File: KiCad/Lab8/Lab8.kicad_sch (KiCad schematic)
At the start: 24 parts, among them M1 Motor, M2 Motor, SW1 Reset, U1 PIC32MX170F256B, U2 74ACT244, U2 SN754410NE

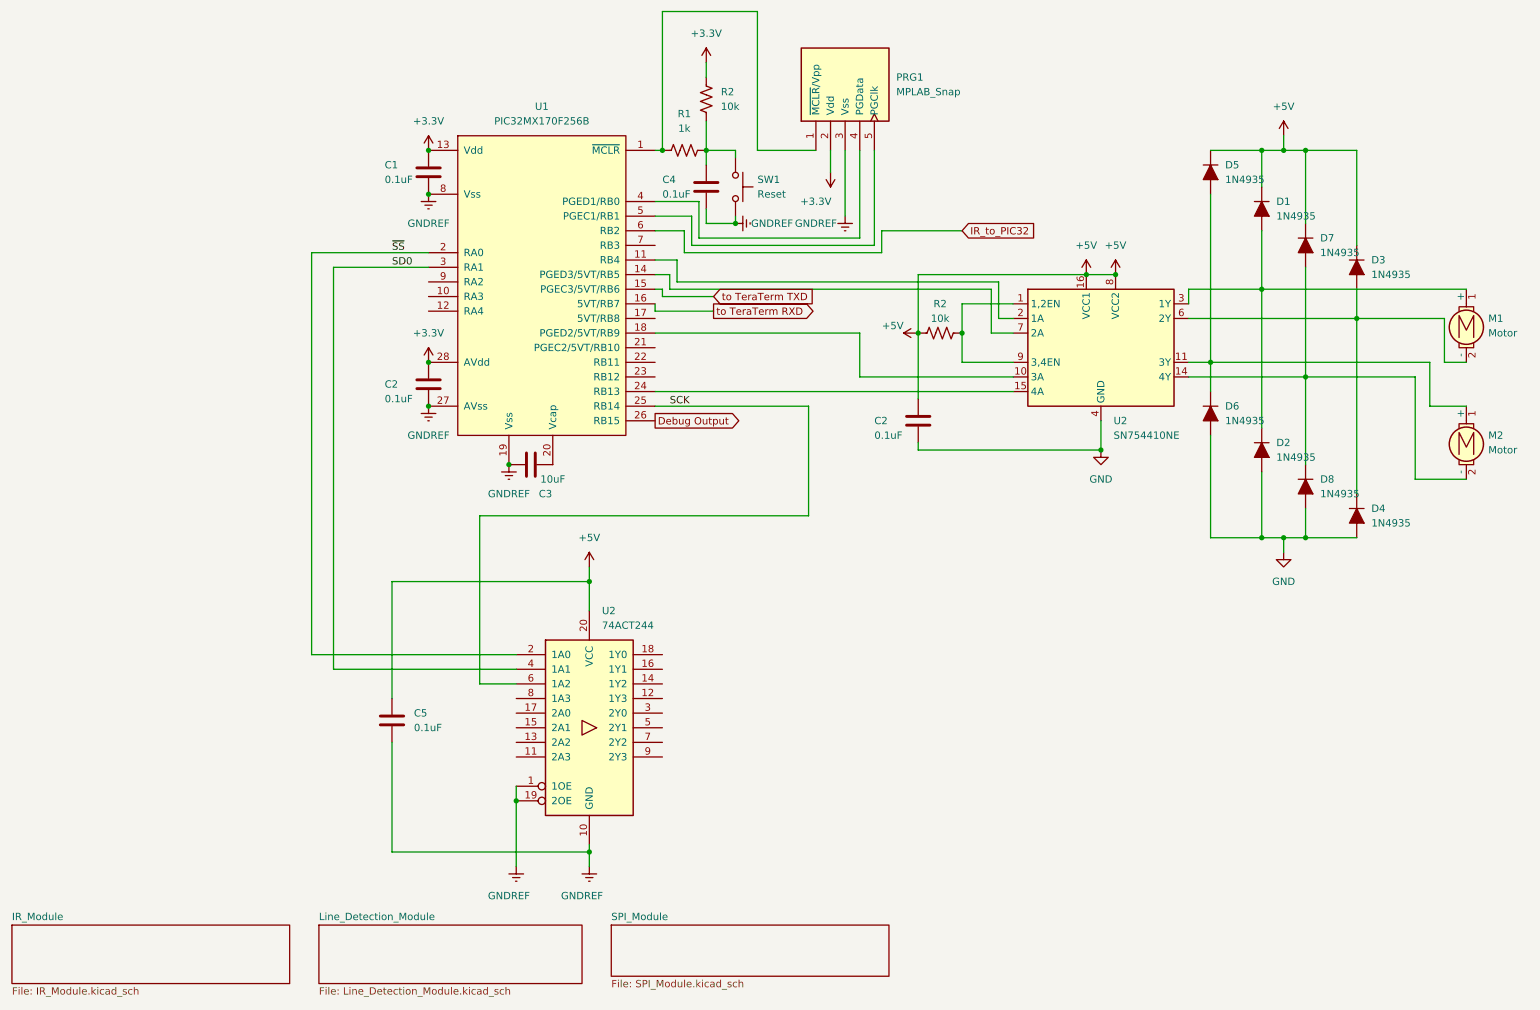
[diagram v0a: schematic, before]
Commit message: Revert "Revert "Update SPI wiring and implement line detection capture""
This reverts commit 9eb00a7cf1ff2e7c6ae798789d116206cfe13d70.
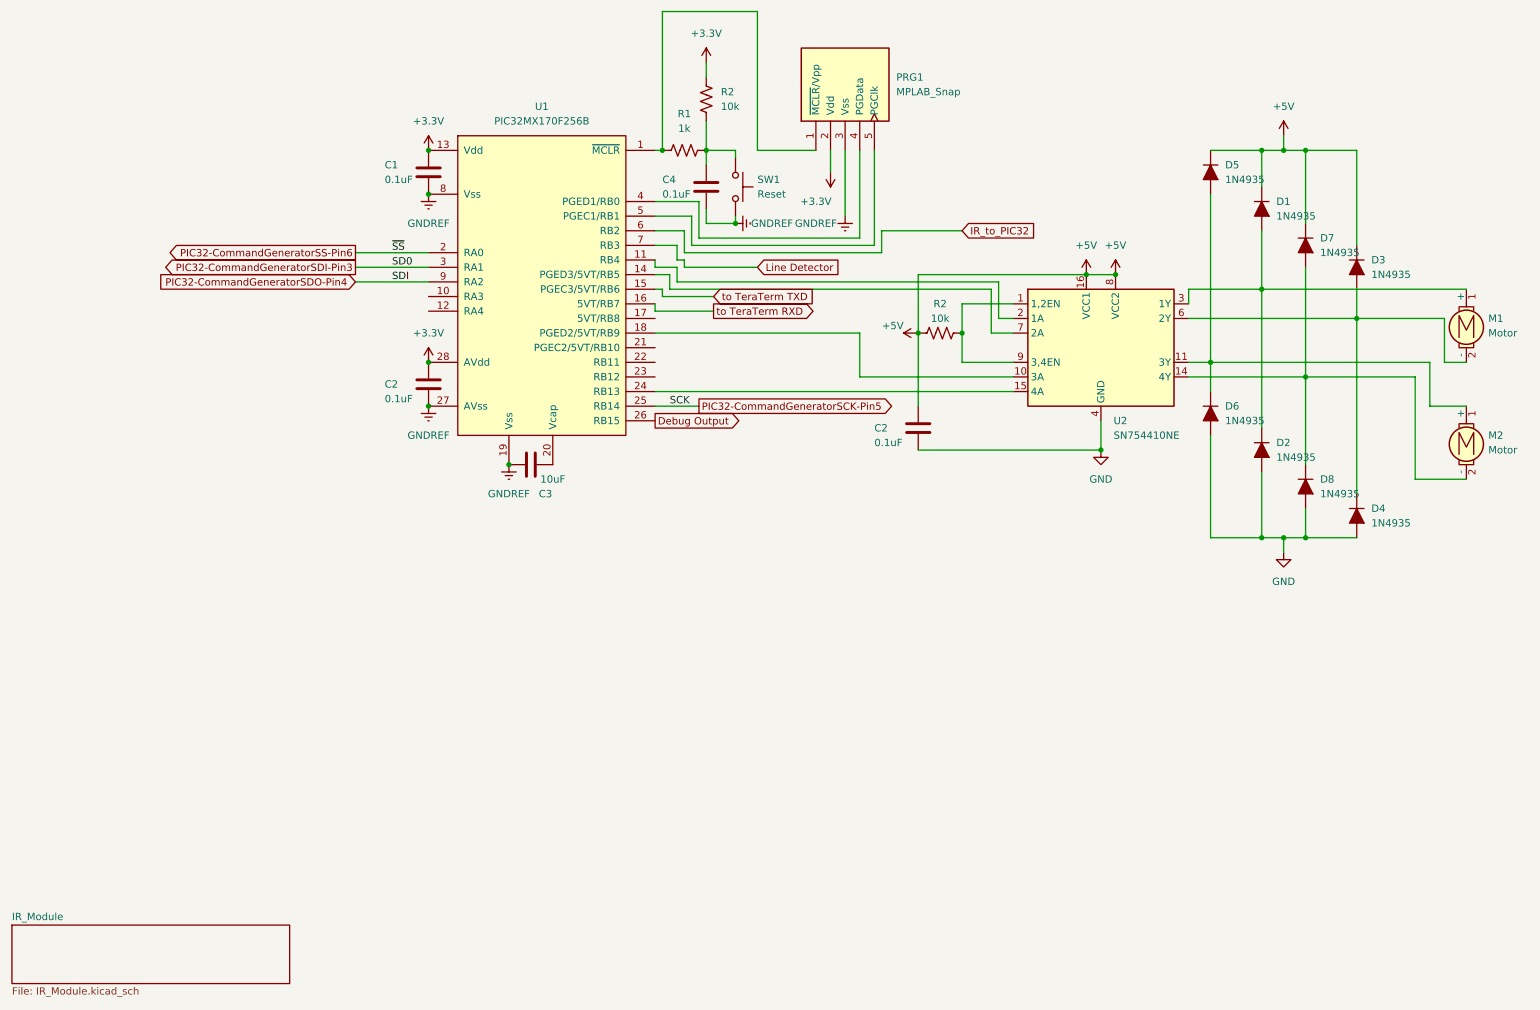
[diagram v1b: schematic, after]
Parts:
- removed C5: 0.1uF, symbol ME218_BaseLib:Cap
- removed U2: 74ACT244, symbol ME218_BaseLib:74xxx244
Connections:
- net Line Detector: now reaches U1.7 (RB3)
- net PIC32-CommandGeneratorSDO-Pin4: now reaches U1.9 (RA2)
- net SCK renamed PIC32-CommandGeneratorSCK-Pin5
- net SD0 renamed PIC32-CommandGeneratorSDI-Pin3
- net ~{SS} renamed PIC32-CommandGeneratorSS-Pin6
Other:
- removed sheet Line_Detection_Module
- removed sheet SPI_Module
- moved on the sheet: C2

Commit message: Revert "Update SPI wiring and implement line detection capture"
This reverts commit 9cbd4223595eda152b008ae8c730017f89a32266.
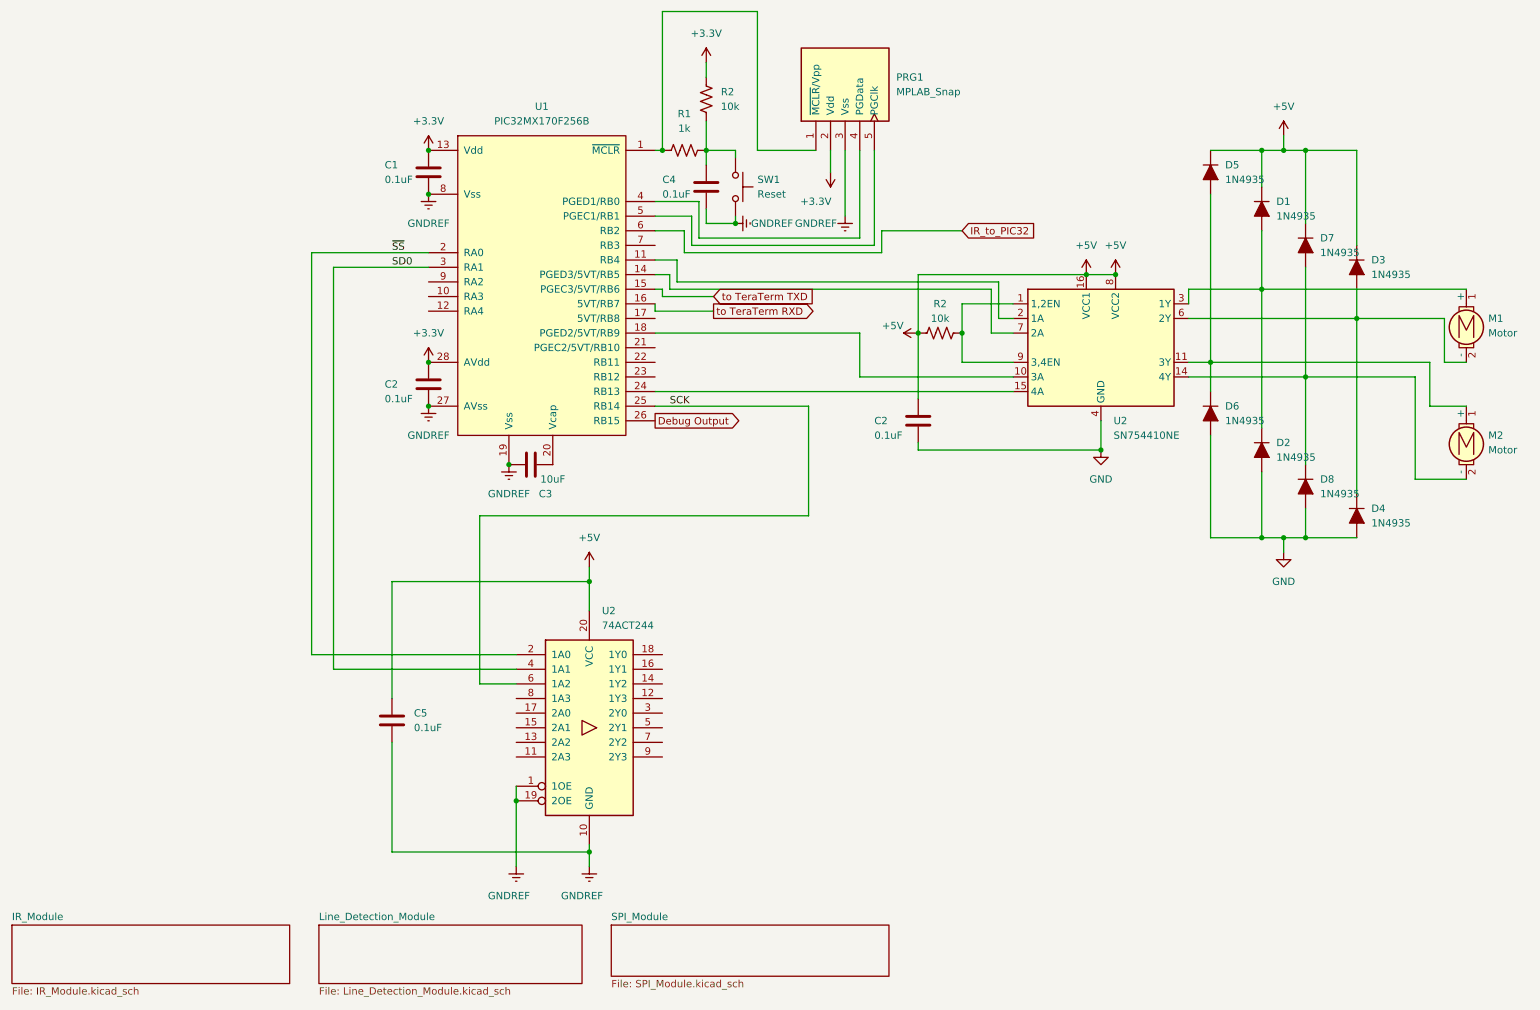
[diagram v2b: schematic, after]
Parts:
- added C5: 0.1uF, symbol ME218_BaseLib:Cap
- added U2: 74ACT244, symbol ME218_BaseLib:74xxx244
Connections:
- net +5V: now also C5.1, U2.20 (VCC)
- net GNDREF: now also C5.2, U2.1 (1OE), U2.10 (GND), U2.19 (2OE)
- net Line Detector: no longer names the net of U1.7 (RB3)
- net PIC32-CommandGeneratorSCK-Pin5 renamed SCK
- net SCK: now also U2.6 (1A2)
- net PIC32-CommandGeneratorSDI-Pin3 renamed SD0
- net SD0: now also U2.4 (1A1)
- net PIC32-CommandGeneratorSDO-Pin4: no longer names the net of U1.9 (RA2)
- net PIC32-CommandGeneratorSS-Pin6 renamed ~{SS}
- net ~{SS}: now also U2.2 (1A0)
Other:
- added sheet Line_Detection_Module (Line_Detection_Module.kicad_sch)
- added sheet SPI_Module (SPI_Module.kicad_sch)
- moved on the sheet: C2
